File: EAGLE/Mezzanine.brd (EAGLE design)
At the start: 83 x 74 mm, 11 parts

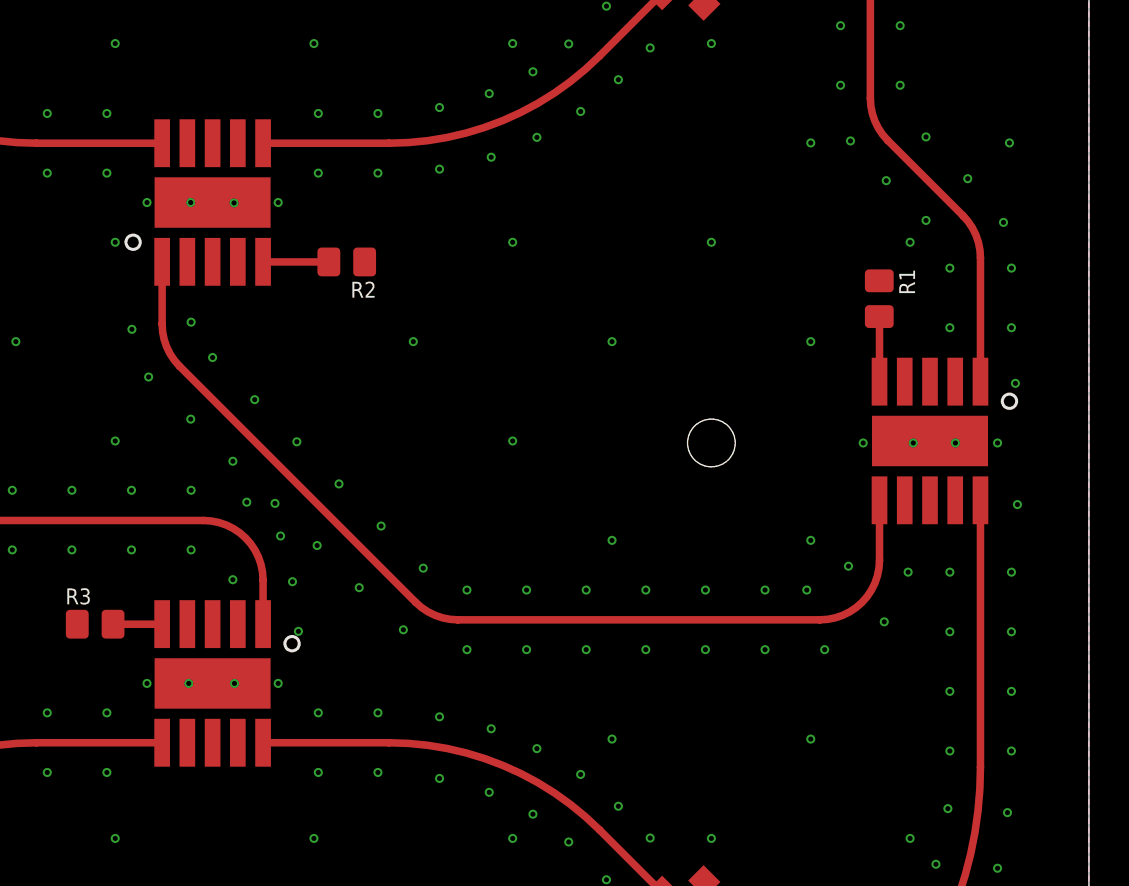
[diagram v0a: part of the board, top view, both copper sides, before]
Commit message: Updated QBA footprints to have no solder mask in order to generate the correct solder paste stencils.
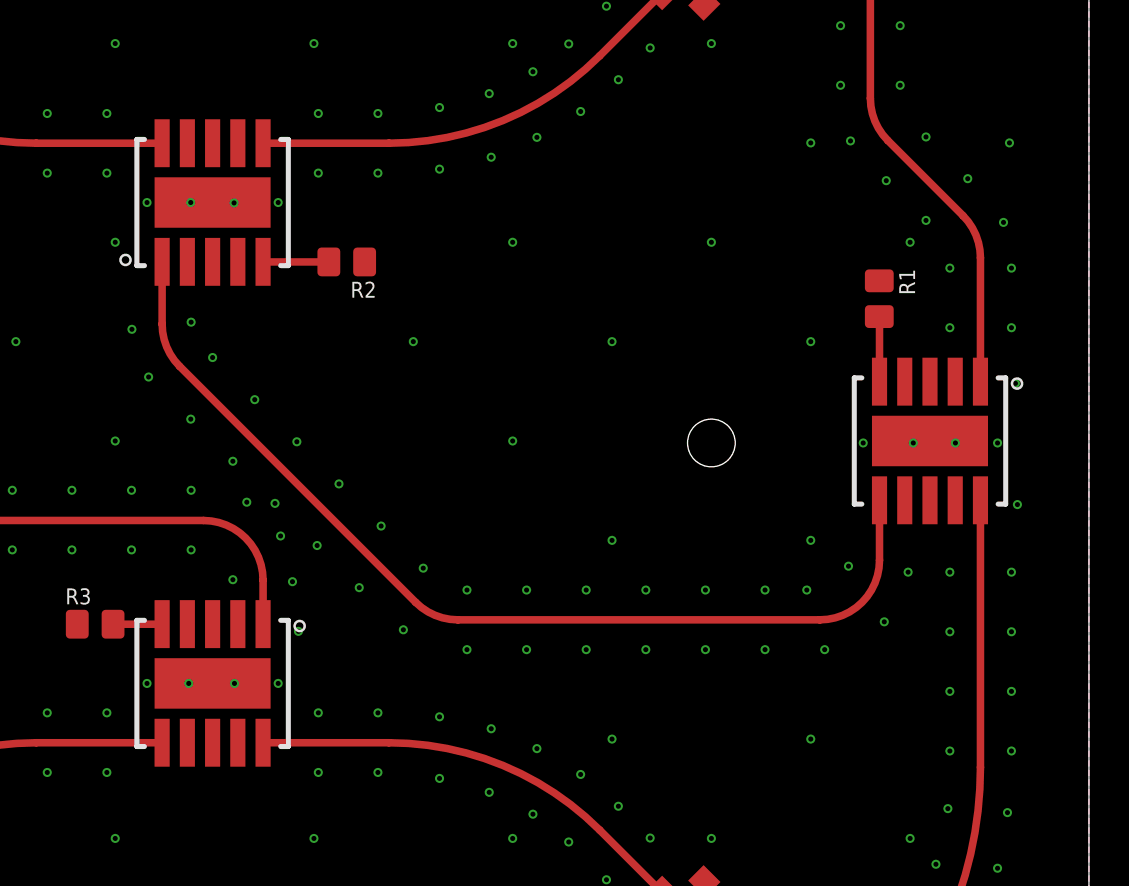
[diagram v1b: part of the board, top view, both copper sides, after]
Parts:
- removed U$10, U$11, U$9: QBA-07+, Mini-Circuits-QBA-07+_Phase-shifter:QBA-07+
- added U1, U2, U3: QBA-07+, U-MiniCirc-QBA-07+_Phase-shifter:QBA-07+
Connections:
- net GND: now also U1.2, U1.3, U1.4, U1.7, U1.8, U1.9, U1.GND-NO-PAD, U2.2, U2.3, U2.4, U2.7, U2.8, U2.9, U2.GND-NO-PAD, U3.2, U3.3, U3.4, U3.7, U3.8, U3.9, U3.GND-NO-PAD; no longer U$10.P$11, U$10.P$2, U$10.P$3, U$10.P$4, U$10.P$7, U$10.P$8, U$10.P$9, U$11.P$11, U$11.P$2, U$11.P$3, U$11.P$4, U$11.P$7, U$11.P$8, U$11.P$9, U$9.P$11, U$9.P$2, U$9.P$3, U$9.P$4, U$9.P$7, U$9.P$8, U$9.P$9
- net N$1: now also U1.1; no longer U$9.P$1
- net N$2: now also U1.6, U2.1; no longer U$10.P$1, U$9.P$6
- net N$3: now also U1.5; no longer U$9.P$5
- net N$4: now also U2.5; no longer U$10.P$5
- net N$5: now also U1.10, U3.1; no longer U$11.P$1, U$9.P$10
- net N$6: now also U3.5; no longer U$11.P$5
- net UHF_0: now also U2.6; no longer U$10.P$6
- net UHF_180: now also U3.6; no longer U$11.P$6
- net UHF_270: now also U3.10; no longer U$11.P$10
- net UHF_90: now also U2.10; no longer U$10.P$10
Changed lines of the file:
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@@
 <grid distance="0.1" unitdist="mm" unit="mm" style="lines" multiple="1" display="yes" altdistance="0.1" altunitdist="mm" altunit="mm"/>
 <layers>
-<layer number="1" name="Top" color="4" fill="1" visible="yes" active="yes"/>
+<layer number="1" name="Top" color="4" fill="1" visible="no" active="yes"/>
 <layer number="2" name="Route2" color="16" fill="1" visible="no" active="yes"/>
 <layer number="3" name="Route3" color="17" fill="1" visible="no" active="no"/>
@@
 <layer number="14" name="Route14" color="22" fill="1" visible="no" active="no"/>
 <layer number="15" name="Route15" color="23" fill="1" visible="no" active="yes"/>
-<layer number="16" name="Bottom" color="1" fill="1" visible="yes" active="yes"/>
-<layer number="17" name="Pads" color="2" fill="1" visible="yes" active="yes"/>
-<layer number="18" name="Vias" color="2" fill="1" visible="yes" active="yes"/>
-<layer number="19" name="Unrouted" color="6" fill="1" visible="yes" active="yes"/>
-<layer number="20" name="Dimension" color="24" fill="1" visible="yes" active="yes"/>
-<layer number="21" name="tPlace" color="7" fill="1" visible="yes" active="yes"/>
-<layer number="22" name="bPlace" color="7" fill="1" visible="yes" active="yes"/>
-<layer number="23" name="tOrigins" color="15" fill="1" visible="yes" active="yes"/>
-<layer number="24" name="bOrigins" color="15" fill="1" visible="yes" active="yes"/>
-<layer number="25" name="tNames" color="7" fill="1" visible="yes" active="yes"/>
-<layer number="26" name="bNames" color="7" fill="1" visible="yes" active="yes"/>
+<layer number="16" name="Bottom" color="1" fill="1" visible="no" active="yes"/>
+<layer number="17" name="Pads" color="2" fill="1" visible="no" active="yes"/>
+<layer number="18" name="Vias" color="2" fill="1" visible="no" active="yes"/>
+<layer number="19" name="Unrouted" color="6" fill="1" visible="no" active="yes"/>
+<layer number="20" name="Dimension" color="24" fill="1" visible="no" active="yes"/>
+<layer number="21" name="tPlace" color="7" fill="1" visible="no" active="yes"/>
+<layer number="22" name="bPlace" color="7" fill="1" visible="no" active="yes"/>
+<layer number="23" name="tOrigins" color="15" fill="1" visible="no" active="yes"/>
+<layer number="24" name="bOrigins" color="15" fill="1" visible="no" active="yes"/>
+<layer number="25" name="tNames" color="7" fill="1" visible="no" active="yes"/>
+<layer number="26" name="bNames" color="7" fill="1" visible="no" active="yes"/>
 <layer number="27" name="tValues" color="7" fill="1" visible="no" active="yes"/>
 <layer number="28" name="bValues" color="7" fill="1" visible="no" active="yes"/>
-<layer number="29" name="tStop" color="7" fill="3" visible="yes" active="yes"/>
-<layer number="30" name="bStop" color="7" fill="6" visible="yes" active="yes"/>
-<layer number="31" name="tCream" color="7" fill="4" visible="no" active="yes"/>
+<layer number="29" name="tStop" color="7" fill="3" visible="no" active="yes"/>
+<layer number="30" name="bStop" color="7" fill="6" visible="no" active="yes"/>
+<layer number="31" name="tCream" color="7" fill="4" visible="yes" active="yes"/>
 <layer number="32" name="bCream" color="7" fill="5" visible="no" active="yes"/>
 <layer number="33" name="tFinish" color="6" fill="3" visible="no" active="yes"/>
@@
 <layer number="44" name="Drills" color="7" fill="1" visible="no" active="yes"/>
 <layer number="45" name="Holes" color="7" fill="1" visible="no" active="yes"/>
-<layer number="46" name="Milling" color="3" fill="1" visible="yes" active="yes"/>
+<layer number="46" name="Milling" color="3" fill="1" visible="no" active="yes"/>
 <layer number="47" name="Measures" color="7" fill="1" visible="no" active="yes"/>
 <layer number="48" name="Document" color="7" fill="1" visible="no" active="yes"/>
@@
 </autorouter>
 <elements>
-<element name="U$9" library="Mini-Circuits-QBA-07+_Phase-shifter" package="QBA-07+" value="QBA-07+" x="86" y="50" smashed="yes" rot="R180"/>
-<element name="U$10" library="Mini-Circuits-QBA-07+_Phase-shifter" package="QBA-07+" value="QBA-07+" x="49.9" y="62" smashed="yes"/>
-<element name="U$11" library="Mini-Circuits-QBA-07+_Phase-shifter" package="QBA-07+" value="QBA-07+" x="49.9" y="37.8" smashed="yes" rot="R180"/>
+<element name="U1" library="U-MiniCirc-QBA-07+_Phase-shifter" package="QBA-07+" value="QBA-07+" x="86" y="50" smashed="yes" rot="R180"/>
+<element name="U2" library="U-MiniCirc-QBA-07+_Phase-shifter" package="QBA-07+" value="QBA-07+" x="49.9" y="62" smashed="yes"/>
+<element name="U3" library="U-MiniCirc-QBA-07+_Phase-shifter" package="QBA-07+" value="QBA-07+" x="49.9" y="37.8" smashed="yes" rot="R180"/>
 <element name="R1" library="oresat-rcl" package=".0805-B-NOSILK" value="50" x="83.45" y="57.16" smashed="yes" rot="R270">
 <attribute name="NAME" x="84.45" y="58.66" size="0.8" layer="25" font="vector" ratio="15" rot="R270"/>
@@
 <signals>
 <signal name="GND">
-<contactref element="U$9" pad="P$2"/>
-<contactref element="U$9" pad="P$4"/>
-<contactref element="U$9" pad="P$8"/>
-<contactref element="U$9" pad="P$9"/>
-<contactref element="U$9" pad="P$11"/>
-<contactref element="U$9" pad="P$3"/>
-<contactref element="U$9" pad="P$7"/>
-<contactref element="U$10" pad="P$2"/>
-<contactref element="U$10" pad="P$4"/>
-<contactref element="U$10" pad="P$8"/>
-<contactref element="U$10" pad="P$9"/>
-<contactref element="U$10" pad="P$11"/>
-<contactref element="U$10" pad="P$3"/>
-<contactref element="U$10" pad="P$7"/>
-<contactref element="U$11" pad="P$2"/>
-<contactref element="U$11" pad="P$4"/>
-<contactref element="U$11" pad="P$8"/>
-<contactref element="U$11" pad="P$9"/>
-<contactref element="U$11" pad="P$11"/>
-<contactref element="U$11" pad="P$3"/>
-<contactref element="U$11" pad="P$7"/>
+<contactref element="U1" pad="2"/>
+<contactref element="U1" pad="4"/>
+<contactref element="U1" pad="8"/>
+<contactref element="U1" pad="9"/>
+<contactref element="U1" pad="GND-NO-PAD"/>
+<contactref element="U1" pad="3"/>
+<contactref element="U1" pad="7"/>
+<contactref element="U2" pad="2"/>
+<contactref element="U2" pad="4"/>
+<contactref element="U2" pad="8"/>
+<contactref element="U2" pad="9"/>
+<contactref element="U2" pad="GND-NO-PAD"/>
+<contactref element="U2" pad="3"/>
+<contactref element="U2" pad="7"/>
+<contactref element="U3" pad="2"/>
+<contactref element="U3" pad="4"/>
+<contactref element="U3" pad="8"/>
+<contactref element="U3" pad="9"/>
+<contactref element="U3" pad="GND-NO-PAD"/>
+<contactref element="U3" pad="3"/>
+<contactref element="U3" pad="7"/>
 <contactref element="R1" pad="1"/>
 <contactref element="R2" pad="1"/>
@@
 </signal>
 <signal name="N$1" class="1">
-<contactref element="U$9" pad="P$1"/>
+<contactref element="U1" pad="1"/>
 <contactref element="U$1" pad="P$1"/>
 <wire x1="87" y1="76" x2="86" y2="76" width="0.38" layer="1"/>
@@
 </signal>
 <signal name="N$2" class="1">
-<contactref element="U$9" pad="P$6"/>
-<contactref element="U$10" pad="P$1"/>
+<contactref element="U1" pad="6"/>
+<contactref element="U2" pad="1"/>
 <wire x1="83.46" y1="47.015" x2="83.46" y2="44" width="0.38" layer="1"/>
 <wire x1="83.46" y1="44" x2="80.46" y2="41" width="0.38" layer="1" curve="-90"/>
@@
 </signal>
 <signal name="N$3" class="1">
-<contactref element="U$9" pad="P$5"/>
+<contactref element="U1" pad="5"/>
 <contactref element="R1" pad="2"/>
 <wire x1="83.45" y1="56.26" x2="83.46" y2="56.235859375" width="0.38" layer="1" curve="-45"/>
@@
 </signal>
 <signal name="N$4" class="1">
-<contactref element="U$10" pad="P$5"/>
+<contactref element="U2" pad="5"/>
 <contactref element="R2" pad="2"/>
 <wire x1="55.75" y1="59.01" x2="52.452071875" y2="59.01" width="0.38" layer="1"/>
@@
 </signal>
 <signal name="N$5" class="1">
-<contactref element="U$11" pad="P$1"/>
-<contactref element="U$9" pad="P$10"/>
+<contactref element="U3" pad="1"/>
+<contactref element="U1" pad="10"/>
 <wire x1="88.54" y1="47.015" x2="88.54" y2="33.58" width="0.38" layer="1"/>
 <wire x1="88.54" y1="33.58" x2="68.96" y2="14" width="0.38" layer="1" curve="-90"/>
@@
 </signal>
 <signal name="N$6" class="1">
-<contactref element="U$11" pad="P$5"/>
+<contactref element="U3" pad="5"/>
 <contactref element="R3" pad="2"/>
 <wire x1="44.89" y1="40.78" x2="47.347928125" y2="40.78" width="0.38" layer="1"/>
@@
 </signal>
 <signal name="UHF_0" class="1">
-<contactref element="U$10" pad="P$6"/>
+<contactref element="U2" pad="6"/>
 <contactref element="U$2" pad="P$1"/>
 <wire x1="52.44" y1="64.985" x2="58.771796875" y2="64.985" width="0.38" layer="1"/>
@@
 </signal>
 <signal name="UHF_90" class="1">
-<contactref element="U$10" pad="P$10"/>
+<contactref element="U2" pad="10"/>
 <contactref element="U$3" pad="P$1"/>
 <wire x1="47.36" y1="64.985" x2="41.0282" y2="64.985" width="0.38" layer="1"/>
@@
 </signal>
 <signal name="UHF_270" class="1">
-<contactref element="U$11" pad="P$10"/>
+<contactref element="U3" pad="10"/>
 <contactref element="U$5" pad="P$1"/>
 <wire x1="52.44" y1="34.815" x2="58.77179375" y2="34.815" width="0.38" layer="1"/>
@@
 </signal>
 <signal name="UHF_180" class="1">
-<contactref element="U$11" pad="P$6"/>
+<contactref element="U3" pad="6"/>
 <contactref element="U$4" pad="P$1"/>
 <wire x1="47.36" y1="34.815" x2="41.028203125" y2="34.815" width="0.38" layer="1"/>
